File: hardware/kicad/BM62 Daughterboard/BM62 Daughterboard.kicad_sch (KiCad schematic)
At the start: 10 parts, among them J1 Conn_2x4, SW1 SW_DIP_x03, U1 BM62

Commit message: Update LED part info for BM62 Daughterboard
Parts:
- D1: Manufacturer_Name Lumex -> Broadcom / Avago; Manufacturer_Part_Number SML-LX1206GC-TR1 -> HSME-C150; Mouser Part Number 696-SML-1206GCTR1 -> 630-HSME-C150; Mouser Price/Stock https://www.mouser.com/ProductDetail/Lumex/SML-LX1206GC-TR1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 -> https://www.mouser.com/ProductDetail/630-HSME-C150
- D2: Manufacturer_Name Lumex -> Broadcom / Avago; Manufacturer_Part_Number SML-LXF1206SRC-TR -> HSMC-C150; Mouser Part Number 696-SML-F1206SRCTR -> 630-HSMC-C150; Mouser Price/Stock https://www.mouser.com/ProductDetail/Lumex/SML-LXF1206SRC-T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 -> https://www.mouser.com/ProductDetail/630-HSMC-C150
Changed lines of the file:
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@@
       (effects (font (size 1.27 1.27)) hide)
     )
-    (property "Datasheet" "https://www.mouser.com/datasheet/2/244/LUMX_S_A0004564595_1-2552013.pdf" (at 119.38 138.43 0)
-      (effects (font (size 1.27 1.27)) hide)
-    )
-    (property "Manufacturer_Name" "Lumex" (at 119.38 138.43 0)
-      (effects (font (size 1.27 1.27)) hide)
-    )
-    (property "Manufacturer_Part_Number" "SML-LX1206GC-TR1" (at 119.38 138.43 0)
-      (effects (font (size 1.27 1.27)) hide)
-    )
-    (property "Mouser Part Number" "696-SML-1206GCTR1" (at 119.38 138.43 0)
-      (effects (font (size 1.27 1.27)) hide)
-    )
-    (property "Mouser Price/Stock" "https://www.mouser.com/ProductDetail/Lumex/SML-LX1206GC-TR1?qs=y33pfUyacG5P560akNmSsQ%3D%3D" (at 119.38 138.43 0)
+    (property "Datasheet" "https://www.mouser.com/datasheet/2/678/av02_0976en-1828033.pdf" (at 119.38 138.43 0)
+      (effects (font (size 1.27 1.27)) hide)
+    )
+    (property "Manufacturer_Name" "Broadcom / Avago" (at 119.38 138.43 0)
+      (effects (font (size 1.27 1.27)) hide)
+    )
+    (property "Manufacturer_Part_Number" "HSME-C150" (at 119.38 138.43 0)
+      (effects (font (size 1.27 1.27)) hide)
+    )
+    (property "Mouser Part Number" "630-HSME-C150" (at 119.38 138.43 0)
+      (effects (font (size 1.27 1.27)) hide)
+    )
+    (property "Mouser Price/Stock" "https://www.mouser.com/ProductDetail/630-HSME-C150" (at 119.38 138.43 0)
       (effects (font (size 1.27 1.27)) hide)
     )
@@
       (effects (font (size 1.27 1.27)) hide)
     )
-    (property "Datasheet" "https://www.mouser.com/datasheet/2/244/LUMX_S_A0001417197_1-2551689.pdf" (at 119.38 128.27 0)
-      (effects (font (size 1.27 1.27)) hide)
-    )
-    (property "Manufacturer_Name" "Lumex" (at 119.38 128.27 0)
-      (effects (font (size 1.27 1.27)) hide)
-    )
-    (property "Manufacturer_Part_Number" "SML-LXF1206SRC-TR" (at 119.38 128.27 0)
-      (effects (font (size 1.27 1.27)) hide)
-    )
-    (property "Mouser Part Number" "696-SML-F1206SRCTR" (at 119.38 128.27 0)
-      (effects (font (size 1.27 1.27)) hide)
-    )
-    (property "Mouser Price/Stock" "https://www.mouser.com/ProductDetail/Lumex/SML-LXF1206SRC-TR?qs=sWJIHVaBZlC2vEnrvCl7Lg%3D%3D" (at 119.38 128.27 0)
-      (effects (font (size 1.27 1.27)) hide)
-    )
+    (property "Datasheet" "https://www.mouser.com/datasheet/2/678/av02-0112en-ds-hsmx-c1xx-29sep2010-1827222.pdf" (at 119.38 128.27 0)
+      (effects (font (size 1.27 1.27)) hide)
+    )
+    (property "Manufacturer_Name" "Broadcom / Avago" (at 119.38 128.27 0)
+      (effects (font (size 1.27 1.27)) hide)
+    )
+    (property "Manufacturer_Part_Number" "HSMC-C150" (at 119.38 128.27 0)
+      (effects (font (size 1.27 1.27)) hide)
+    )
+    (property "Mouser Part Number" "630-HSMC-C150" (at 119.38 128.27 0)
+      (effects (font (size 1.27 1.27)) hide)
+    )
+    (property "Mouser Price/Stock" "https://www.mouser.com/ProductDetail/630-HSMC-C150" (at 119.38 128.27 0)
+      (effects (font (size 1.27 1.27)) hide)
+    )

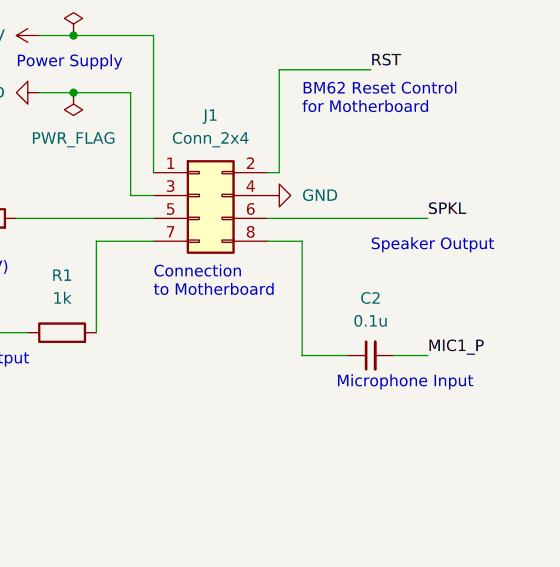
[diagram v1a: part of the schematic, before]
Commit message: BM62 daughterboard adjustment to connector ground pins
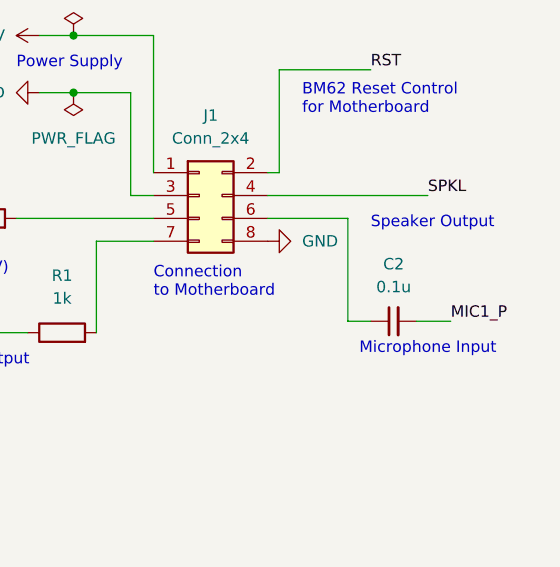
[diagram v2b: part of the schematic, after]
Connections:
- net GND: now also J1.8 (Pin_8); no longer J1.4 (Pin_4)
- net SPKL: now also J1.4 (Pin_4); no longer J1.6 (Pin_6)
- net at C2.1: now also J1.6 (Pin_6); no longer J1.8 (Pin_8)
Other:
- moved on the sheet: C2
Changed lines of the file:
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@@
+    (stroke (width 0) (type default))
+  )
+  (wire (pts (xy 203.2 77.47) (xy 194.31 77.47))
     (stroke (width 0) (type default))
   )
@@
     (stroke (width 0) (type default))
   )
-  (wire (pts (xy 208.28 92.71) (xy 212.09 92.71))
-    (stroke (width 0) (type default))
-  )
-  (wire (pts (xy 194.31 80.01) (xy 198.12 80.01))
+  (wire (pts (xy 210.82 88.9) (xy 214.63 88.9))
     (stroke (width 0) (type default))
   )
@@
     (stroke (width 0) (type default))
   )
-  (wire (pts (xy 198.12 80.01) (xy 198.12 92.71))
+  (wire (pts (xy 203.2 77.47) (xy 203.2 88.9))
     (stroke (width 0) (type default))
   )
@@
     (stroke (width 0) (type default))
   )
-  (wire (pts (xy 194.31 77.47) (xy 212.09 77.47))
-    (stroke (width 0) (type default))
-  )
   (wire (pts (xy 118.11 90.17) (xy 115.57 90.17))
     (stroke (width 0) (type default))
@@
     (stroke (width 0) (type default))
   )
-  (wire (pts (xy 198.12 92.71) (xy 203.2 92.71))
+  (wire (pts (xy 194.31 74.93) (xy 212.09 74.93))
+    (stroke (width 0) (type default))
+  )
+  (wire (pts (xy 203.2 88.9) (xy 205.74 88.9))
     (stroke (width 0) (type default))
   )
@@
     (effects (font (size 1.27 1.27)) (justify left bottom))
   )
-  (text "Speaker Output" (at 205.74 81.28 0)
-    (effects (font (size 1.27 1.27)) (justify left bottom))
-  )
-  (text "Microphone Input" (at 201.93 96.52 0)
+  (text "Speaker Output" (at 205.74 78.74 0)
+    (effects (font (size 1.27 1.27)) (justify left bottom))
+  )
+  (text "Microphone Input" (at 204.47 92.71 0)
     (effects (font (size 1.27 1.27)) (justify left bottom))
   )
@@
     (effects (font (size 1.27 1.27)) (justify left bottom))
   )
-  (label "SPKL" (at 212.09 77.47 0) (fields_autoplaced)
+  (label "SPKL" (at 212.09 74.93 0) (fields_autoplaced)
     (effects (font (size 1.27 1.27)) (justify left bottom))
   )
@@
     (effects (font (size 1.27 1.27)) (justify right bottom))
   )
-  (label "MIC1_P" (at 212.09 92.71 0) (fields_autoplaced)
+  (label "MIC1_P" (at 214.63 88.9 0) (fields_autoplaced)
     (effects (font (size 1.27 1.27)) (justify left bottom))
   )
@@
     )
   )
-  (symbol (lib_id "Device:C_Small") (at 205.74 92.71 90) (unit 1)
-    (in_bom yes) (on_board yes) (dnp no) (fields_autoplaced)
-    (property "Reference" "C2" (at 205.7463 86.36 90)
-      (effects (font (size 1.27 1.27)))
-    )
-    (property "Value" "0.1u" (at 205.7463 88.9 90)
-      (effects (font (size 1.27 1.27)))
-    )
-    (property "Footprint" "Capacitor_SMD:C_1206_3216Metric_Pad1.33x1.80mm_HandSolder" (at 205.74 92.71 0)
-      (effects (font (size 1.27 1.27)) hide)
-    )
-    (property "Datasheet" "https://www.mouser.com/datasheet/2/447/KEM_C1007_X8R_ULTRA_150C_SMD-3316375.pdf" (at 205.74 92.71 0)
-      (effects (font (size 1.27 1.27)) hide)
-    )
-    (property "Manufacturer_Name" "KEMET" (at 205.74 92.71 0)
-      (effects (font (size 1.27 1.27)) hide)
-    )
-    (property "Manufacturer_Part_Number" "C1206C104J4HACTU" (at 205.74 92.71 0)
-      (effects (font (size 1.27 1.27)) hide)
-    )
-    (property "Mouser Part Number" "80-C1206C104J4HACTU" (at 205.74 92.71 0)
-      (effects (font (size 1.27 1.27)) hide)
-    )
-    (property "Mouser Price/Stock" "https://www.mouser.com/ProductDetail/KEMET/C1206C104J4HACTU?qs=W0yvOO0ixfH3SzteelzlzQ%3D%3D" (at 205.74 92.71 0)
+  (symbol (lib_id "Device:C_Small") (at 208.28 88.9 90) (unit 1)
+    (in_bom yes) (on_board yes) (dnp no) (fields_autoplaced)
+    (property "Reference" "C2" (at 208.2863 82.55 90)
+      (effects (font (size 1.27 1.27)))
+    )
+    (property "Value" "0.1u" (at 208.2863 85.09 90)
+      (effects (font (size 1.27 1.27)))
+    )
+    (property "Footprint" "Capacitor_SMD:C_1206_3216Metric_Pad1.33x1.80mm_HandSolder" (at 208.28 88.9 0)
+      (effects (font (size 1.27 1.27)) hide)
+    )
+    (property "Datasheet" "https://www.mouser.com/datasheet/2/447/KEM_C1007_X8R_ULTRA_150C_SMD-3316375.pdf" (at 208.28 88.9 0)
+      (effects (font (size 1.27 1.27)) hide)
+    )
+    (property "Manufacturer_Name" "KEMET" (at 208.28 88.9 0)
+      (effects (font (size 1.27 1.27)) hide)
+    )
+    (property "Manufacturer_Part_Number" "C1206C104J4HACTU" (at 208.28 88.9 0)
+      (effects (font (size 1.27 1.27)) hide)
+    )
+    (property "Mouser Part Number" "80-C1206C104J4HACTU" (at 208.28 88.9 0)
+      (effects (font (size 1.27 1.27)) hide)
+    )
+    (property "Mouser Price/Stock" "https://www.mouser.com/ProductDetail/KEMET/C1206C104J4HACTU?qs=W0yvOO0ixfH3SzteelzlzQ%3D%3D" (at 208.28 88.9 0)
       (effects (font (size 1.27 1.27)) hide)
     )
@@
         (path "/a7594a56-61d6-454c-81f6-369994de0160"
           (reference "#FLG04") (unit 1)
-        )
-      )
-    )
-  )
-  (symbol (lib_id "power:GND") (at 194.31 74.93 90) (unit 1)
-    (in_bom yes) (on_board yes) (dnp no) (fields_autoplaced)
-    (property "Reference" "#PWR06" (at 200.66 74.93 0)
-      (effects (font (size 1.27 1.27)) hide)
-    )
-    (property "Value" "GND" (at 198.12 74.93 90)
-      (effects (font (size 1.27 1.27)) (justify right))
-    )
-    (property "Footprint" "" (at 194.31 74.93 0)
-      (effects (font (size 1.27 1.27)) hide)
-    )
-    (property "Datasheet" "" (at 194.31 74.93 0)
-      (effects (font (size 1.27 1.27)) hide)
-    )
-    (pin "1")
-    (instances
-      (project "BM62 Daughterboard"
-        (path "/a7594a56-61d6-454c-81f6-369994de0160"
-          (reference "#PWR06") (unit 1)
         )
       )
@@
         )
       )
+    )
+  )
+  (symbol (lib_id "power:GND") (at 194.31 80.01 90) (unit 1)
+    (in_bom yes) (on_board yes) (dnp no) (fields_autoplaced)
+    (property "Reference" "#PWR04" (at 200.66 80.01 0)
+      (effects (font (size 1.27 1.27)) hide)
+    )
+    (property "Value" "GND" (at 198.12 80.01 90)
+      (effects (font (size 1.27 1.27)) (justify right))
+    )
+    (property "Footprint" "" (at 194.31 80.01 0)
+      (effects (font (size 1.27 1.27)) hide)
+    )
+    (property "Datasheet" "" (at 194.31 80.01 0)
+      (effects (font (size 1.27 1.27)) hide)
+    )
+    (pin "1")
+    (instances
+      (project "BM62 Daughterboard"
+        (path "/a7594a56-61d6-454c-81f6-369994de0160"
+          (reference "#PWR04") (unit 1)
+        )
+      )

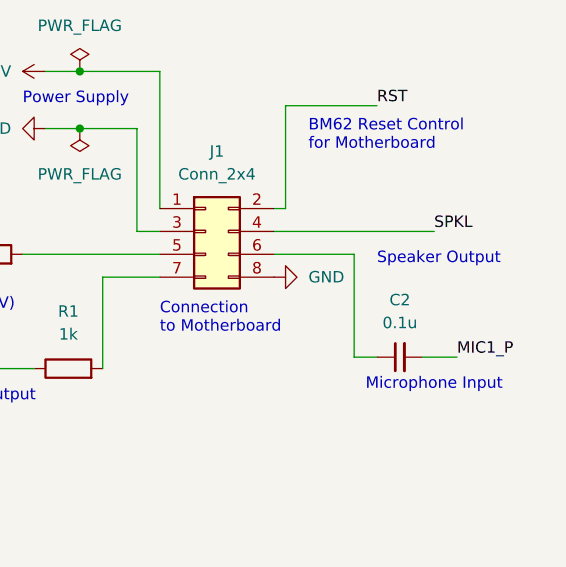
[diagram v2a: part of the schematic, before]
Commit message: BM62 Daughterboard fixes
* Fixed some pin assignments that I must have messed up previously
* Added JLCPCB part numbers for parts on the bottom side
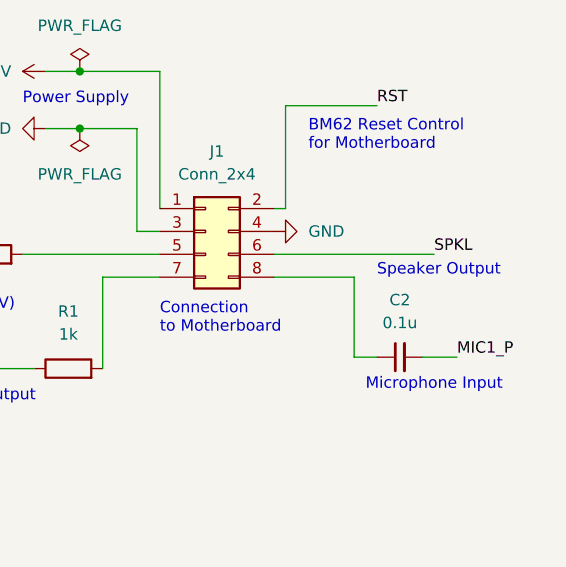
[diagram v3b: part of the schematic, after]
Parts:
- C2: JLCPCB Part# (none) -> C24497
- R1, R2: JLCPCB Part# (none) -> C4410
- R3: JLCPCB Part# (none) -> C17944
- U1: JLCPCB Part# (none) -> C610451
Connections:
- net GND: now also J1.4 (Pin_4); no longer J1.8 (Pin_8)
- net SPKL: now also J1.6 (Pin_6); no longer J1.4 (Pin_4)
- net at C2.1: now also J1.8 (Pin_8); no longer J1.6 (Pin_6)
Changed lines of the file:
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@@
     (stroke (width 0) (type default))
   )
-  (wire (pts (xy 203.2 77.47) (xy 194.31 77.47))
+  (wire (pts (xy 203.2 80.01) (xy 194.31 80.01))
     (stroke (width 0) (type default))
   )
@@
     (stroke (width 0) (type default))
   )
-  (wire (pts (xy 203.2 77.47) (xy 203.2 88.9))
+  (wire (pts (xy 203.2 80.01) (xy 203.2 88.9))
     (stroke (width 0) (type default))
   )
@@
     (stroke (width 0) (type default))
   )
-  (wire (pts (xy 194.31 74.93) (xy 212.09 74.93))
+  (wire (pts (xy 194.31 77.47) (xy 212.09 77.47))
     (stroke (width 0) (type default))
   )
@@
     (effects (font (size 1.27 1.27)) (justify left bottom))
   )
-  (text "Speaker Output" (at 205.74 78.74 0)
+  (text "Speaker Output" (at 205.74 80.01 0)
     (effects (font (size 1.27 1.27)) (justify left bottom))
   )
@@
     (effects (font (size 1.27 1.27)) (justify left bottom))
   )
-  (label "SPKL" (at 212.09 74.93 0) (fields_autoplaced)
+  (label "SPKL" (at 212.09 77.47 0) (fields_autoplaced)
     (effects (font (size 1.27 1.27)) (justify left bottom))
   )
@@
     )
     (property "Mouser Price/Stock" "https://www.mouser.com/ProductDetail/630-HSME-C150" (at 119.38 138.43 0)
+      (effects (font (size 1.27 1.27)) hide)
+    )
+    (property "JLCPCB Part#" "" (at 119.38 138.43 0)
       (effects (font (size 1.27 1.27)) hide)
     )
@@
       (effects (font (size 1.27 1.27)) hide)
     )
+    (property "JLCPCB Part#" "C24497" (at 208.28 88.9 0)
+      (effects (font (size 1.27 1.27)) hide)
+    )
     (pin "2")
     (pin "1")
@@
     )
     (property "Mouser Price/Stock" "https://www.mouser.com/ProductDetail/Bourns/CR1206-FX-1001ELF?qs=sGAEpiMZZMvdGkrng054t%2Fh5BnJxeWSzM1Z%2Fr5f8MxE%3D" (at 171.45 90.17 0)
+      (effects (font (size 1.27 1.27)) hide)
+    )
+    (property "JLCPCB Part#" "C4410" (at 171.45 90.17 0)
       (effects (font (size 1.27 1.27)) hide)
     )
@@
     )
     (property "Mouser Price/Stock" "https://www.mouser.com/ProductDetail/Bourns/CR1206-FX-1001ELF?qs=sGAEpiMZZMvdGkrng054t%2Fh5BnJxeWSzM1Z%2Fr5f8MxE%3D" (at 162.56 77.47 0)
+      (effects (font (size 1.27 1.27)) hide)
+    )
+    (property "JLCPCB Part#" "C4410" (at 162.56 77.47 0)
       (effects (font (size 1.27 1.27)) hide)
     )
@@
     )
     (property "Mouser Price/Stock" "https://www.mouser.com/ProductDetail/CUI-Devices/DS04-254-1-03BK-SMT?qs=wnTfsH77Xs6AM9RonXx4xg%3D%3D" (at 171.45 137.16 0)
+      (effects (font (size 1.27 1.27)) hide)
+    )
+    (property "JLCPCB Part#" "" (at 171.45 137.16 0)
       (effects (font (size 1.27 1.27)) hide)
     )
@@
       (effects (font (size 1.27 1.27)) hide)
     )
+    (property "JLCPCB Part#" "" (at 73.66 132.08 0)
+      (effects (font (size 1.27 1.27)) hide)
+    )
     (pin "1")
     (pin "2")
@@
     )
     (property "Mouser Price/Stock" "https://www.mouser.com/ProductDetail/538-90122-0124" (at 186.69 74.93 0)
+      (effects (font (size 1.27 1.27)) hide)
+    )
+    (property "JLCPCB Part#" "" (at 186.69 74.93 0)
       (effects (font (size 1.27 1.27)) hide)
     )
@@
       (effects (font (size 1.27 1.27)) hide)
     )
+    (property "JLCPCB Part#" "" (at 119.38 128.27 0)
+      (effects (font (size 1.27 1.27)) hide)
+    )
     (pin "1")
     (pin "2")
@@
     )
     (property "Mouser Price/Stock" "https://www.mouser.com/ProductDetail/Microchip-Technology/BM62SPKS1MC2-0001AA?qs=sGAEpiMZZMu3sxpa5v1qrtgrs%252B7l%252BXQB551NanK51K4%3D" (at 86.36 74.93 0)
+      (effects (font (size 1.27 1.27)) hide)
+    )
+    (property "JLCPCB Part#" "C610451" (at 86.36 74.93 0)
       (effects (font (size 1.27 1.27)) hide)
     )
@@
       (effects (font (size 1.27 1.27)) hide)
     )
+    (property "JLCPCB Part#" "C17944" (at 154.94 77.47 0)
+      (effects (font (size 1.27 1.27)) hide)
+    )
     (pin "2")
     (pin "1")
@@
         (path "/a7594a56-61d6-454c-81f6-369994de0160"
           (reference "R3") (unit 1)
+        )
+      )
+    )
+  )
+  (symbol (lib_id "power:GND") (at 194.31 74.93 90) (unit 1)
+    (in_bom yes) (on_board yes) (dnp no) (fields_autoplaced)
+    (property "Reference" "#PWR06" (at 200.66 74.93 0)
+      (effects (font (size 1.27 1.27)) hide)
+    )
+    (property "Value" "GND" (at 198.12 74.93 90)
+      (effects (font (size 1.27 1.27)) (justify right))
+    )
+    (property "Footprint" "" (at 194.31 74.93 0)
+      (effects (font (size 1.27 1.27)) hide)
+    )
+    (property "Datasheet" "" (at 194.31 74.93 0)
+      (effects (font (size 1.27 1.27)) hide)
+    )
+    (pin "1")
+    (instances
+      (project "BM62 Daughterboard"
+        (path "/a7594a56-61d6-454c-81f6-369994de0160"
+          (reference "#PWR06") (unit 1)
         )
       )
@@
         )
       )
-    )
-  )
-  (symbol (lib_id "power:GND") (at 194.31 80.01 90) (unit 1)
-    (in_bom yes) (on_board yes) (dnp no) (fields_autoplaced)
-    (property "Reference" "#PWR04" (at 200.66 80.01 0)
-      (effects (font (size 1.27 1.27)) hide)
-    )
-    (property "Value" "GND" (at 198.12 80.01 90)
-      (effects (font (size 1.27 1.27)) (justify right))
-    )
-    (property "Footprint" "" (at 194.31 80.01 0)
-      (effects (font (size 1.27 1.27)) hide)
-    )
-    (property "Datasheet" "" (at 194.31 80.01 0)
-      (effects (font (size 1.27 1.27)) hide)
-    )
-    (pin "1")
-    (instances
-      (project "BM62 Daughterboard"
-        (path "/a7594a56-61d6-454c-81f6-369994de0160"
-          (reference "#PWR04") (unit 1)
-        )
-      )

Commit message: Clean up BM62 Daughterboard KiCad project
* Use generalized names for project-level symbol/footprint/model libraries.
* Remove a 3D model that belongs in the SymacSys_Parts library.
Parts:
- U1: footprint BM62 Daughterboard:Microchip BM62 -> Project Footprints:Microchip BM62; symbol BM62 Daughterboard:Microchip BM62 -> Project Symbols:Microchip BM62
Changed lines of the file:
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@@
     )
   )
-  (symbol (lib_id "BM62 Daughterboard:Microchip BM62") (at 86.36 74.93 0) (unit 1)
+  (symbol (lib_id "Project Symbols:Microchip BM62") (at 86.36 74.93 0) (unit 1)
     (in_bom yes) (on_board yes) (dnp no) (fields_autoplaced)
     (property "Reference" "U1" (at 97.4441 41.91 0)
@@
       (effects (font (size 1.27 1.27)) (justify left))
     )
-    (property "Footprint" "BM62 Daughterboard:Microchip BM62" (at 86.36 74.93 0)
+    (property "Footprint" "Project Footprints:Microchip BM62" (at 86.36 74.93 0)
       (effects (font (size 1.27 1.27)) hide)
     )
